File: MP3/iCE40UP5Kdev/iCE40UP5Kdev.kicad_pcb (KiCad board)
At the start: 2 copper layers, 27.9 x 52.4 mm, 51 parts, among them J1 USB4105-GF-A, J2 Left, J3 Right, U1 W25Q32JV, U2 MIC5365-1-2YD5, U3 MIC5318-3-3YD5, U4 ICE40UP5K-SG48ITR, X1 IQXO-791

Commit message: Rev.1 Layout
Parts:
- moved S3 42.7 mm to (164.3, 85.6)
- moved C1 41.3 mm to (153.8, 95.9)
- moved R2 39.8 mm to (163.6, 101.3), turned to 90 degrees
- moved R5 38.8 mm to (157.7, 70.5), turned to 90 degrees
- moved R7 33.4 mm to (166.4, 68.5), turned to -90 degrees
- moved C2 33.2 mm to (151.2, 92.0), turned to -90 degrees
- moved C13 32.8 mm to (158.2, 73.0), turned to -90 degrees
- moved C7 32.0 mm to (154.0, 70.6), turned to 90 degrees
- moved D1 31.9 mm to (164.9, 65.7), turned to -90 degrees
- moved R12 28.7 mm to (154.2, 72.8), turned to -90 degrees
- moved R9 27.9 mm to (165.4, 68.5), turned to -90 degrees
- moved R8 27.1 mm to (164.4, 68.5), turned to -90 degrees
- moved C10 26.7 mm to (159.2, 83.9), turned to 90 degrees
- moved R20 25.8 mm to (164.3, 82.6)
- moved R6 24.9 mm to (156.6, 70.5), turned to 90 degrees
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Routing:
- net +5V: track 53.1 -> 195.8 mm, vias 0 -> 2
- net +3V3: track 115.5 -> 204.9 mm, vias 0 -> 11
- net Net-(J1-D--PadA7): track 2.70 -> 81.5 mm, vias 0 -> 2
- net Net-(J1-D+-PadA6): track 5.57 -> 70.7 mm, vias 2 -> 7
- net /RGB2: track 0.00 -> 59.1 mm, vias 0 -> 5
- net /RGB1: track 0.00 -> 56.6 mm, vias 0 -> 5
- net /RGB0: track 0.00 -> 51.9 mm, vias 0 -> 5
- net GND: track 18.9 -> 56.0 mm, vias 7 -> 24
- net /IOT_48b: track 0.00 -> 32.7 mm, vias 0 -> 2
- net /IOT_45a_G1: track 0.00 -> 30.4 mm
- net /IOT_46b_G0: track 0.00 -> 30.3 mm
- net /IOT_44b: track 0.00 -> 26.6 mm
- net Net-(U1-~{CS}): track 0.00 -> 25.1 mm, vias 0 -> 2
- net +1V2: track 3.07 -> 27.7 mm, vias 0 -> 4
- net Net-(U1-DO/IO1): track 0.00 -> 23.9 mm, vias 0 -> 2
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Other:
- board size 27.9 x 52.4 mm -> 29.6 x 52.2 mm

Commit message: Final Design with PinHeader Labels + Graphics
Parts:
- added G***: LOGO, LOGO, B.Cu at (154.9, 95.2)
- added OlinLogo: G***, Eclectronics:OlinLogo, F.Cu at (165.7, 101.7)
- moved C14 8.14 mm to (157.4, 83.8), turned to 90 degrees
- moved U2 5.13 mm to (153.5, 97.7)
- moved C1 5.01 mm to (153.4, 100.9)
- moved R20 4.80 mm to (164.3, 87.4), turned to 180 degrees
- moved C2 3.55 mm to (153.4, 94.8), turned to 0 degrees
- moved R18 1.97 mm to (157.0, 86.3)
- moved R2 1.69 mm to (162.6, 99.9)
- moved C15 1.67 mm to (154.6, 87.1)
- moved R19 1.53 mm to (161.7, 69.5)
- moved S3 1.28 mm to (164.3, 84.3)
- moved D4 1.12 mm to (153.0, 83.0)
- moved C11 1.11 mm to (153.9, 82.9)
- moved C9 0.66 mm to (162.2, 73.9), turned to -90 degrees
- moved C10 0.46 mm to (159.2, 83.4)
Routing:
- net +5V: track 195.8 -> 181.3 mm
- net +3V3: track 204.9 -> 195.7 mm, vias 11 -> 12
- net /IOT_45a_G1: track 30.4 -> 34.0 mm
- net /IOT_50b: track 10.0 -> 13.3 mm, vias 0 -> 2
- net /IOT_37a: track 18.8 -> 16.5 mm
- net /IOT_49a: track 30.6 -> 32.6 mm
- net /IOT_51a: track 17.0 -> 19.0 mm
- net /IOB_3b_G6: track 29.2 -> 31.2 mm
- net /IOB_2a: track 19.8 -> 21.7 mm
- net /IOB_5a: track 26.5 -> 28.4 mm
- net GND: track 56.0 -> 54.2 mm, vias 24 -> 25
- net /IOB_0a: track 24.3 -> 26.1 mm
- net +1V2: track 27.7 -> 29.5 mm
- net Net-(D4-K): track 4.32 -> 2.80 mm
- net /IOB_4a: track 17.6 -> 19.1 mm
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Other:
- board size 29.6 x 52.2 mm -> 32.2 x 52.2 mm
- board text added: "0A"
- board text added: "13B"
- board text added: "18A"
- board text added: "20A"
- board text added: "29b"
- board text added: "2A"
- board text added: "31b"
- board text added: "36b"
- board text added: "37a"
- board text added: "38b"
- board text added: "39a"
- board text added: "3B G6"
- board text added: "3V3"
- board text added: "41a"
- board text added: "42b"
- board text added: "43a"
- board text added: "44b"
- board text added: "45A G1"
- board text added: "46b G0"
- board text added: "48B"
- board text added: "49A"
- board text added: "4A"
- board text added: "5A"
- board text added: "5V"
- board text added: "6A"
- board text added: "8A"
- board text added: "9B"
- board text added: "BOOT"
- board text added: "By"
- board text added: "Designed Jun Park"
- board text added: "GND"
- board text added: "LED"
- board text added: "PWR"
- board text added: "RGB"
- board text added: "RGB 0"
- board text added: "RGB 1"
- board text added: "RGB 2"
- board text added: "RST"
- board text added: "Rev 1.0"
- board text added: "SW"
- board text added: "ice40 FPGA Dev Board"

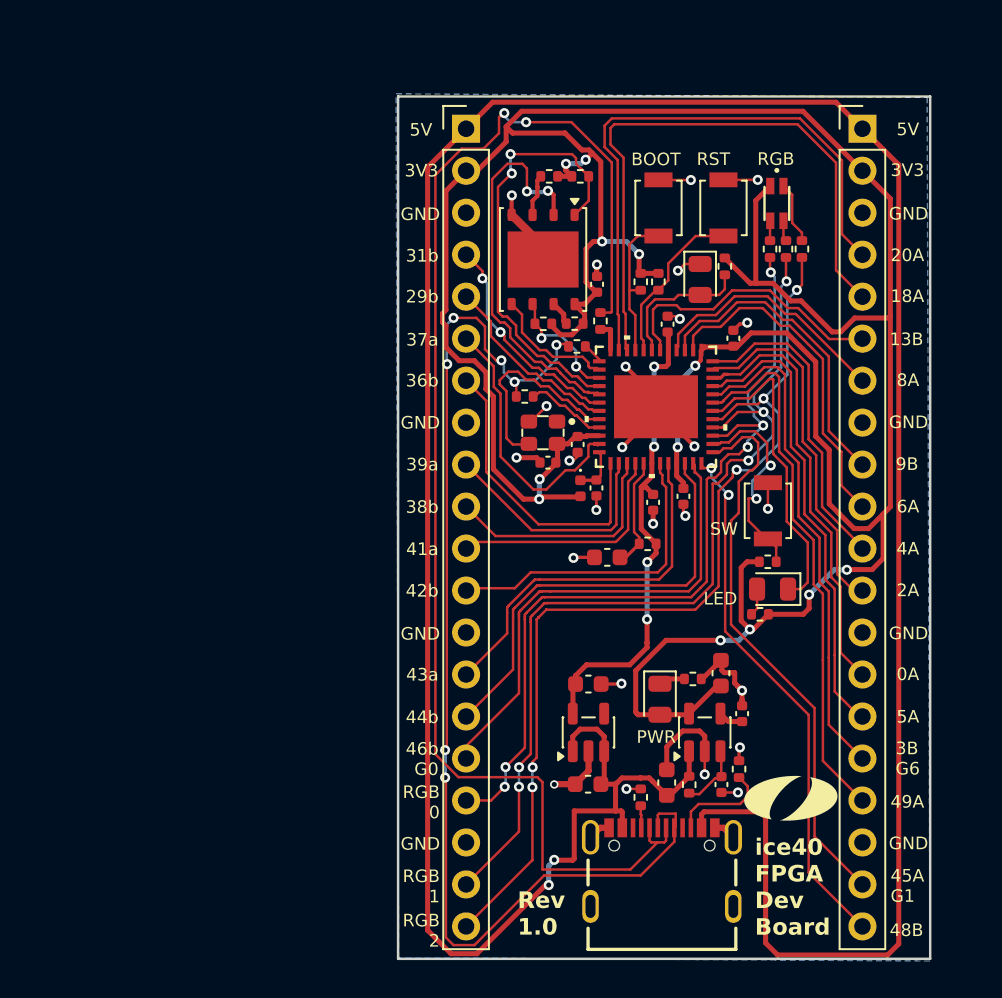
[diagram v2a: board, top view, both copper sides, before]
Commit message: Implementing Feedback
- Made USB D+, D- on one plane and made the path shorter
- Used correct footprint for FPGA Chip
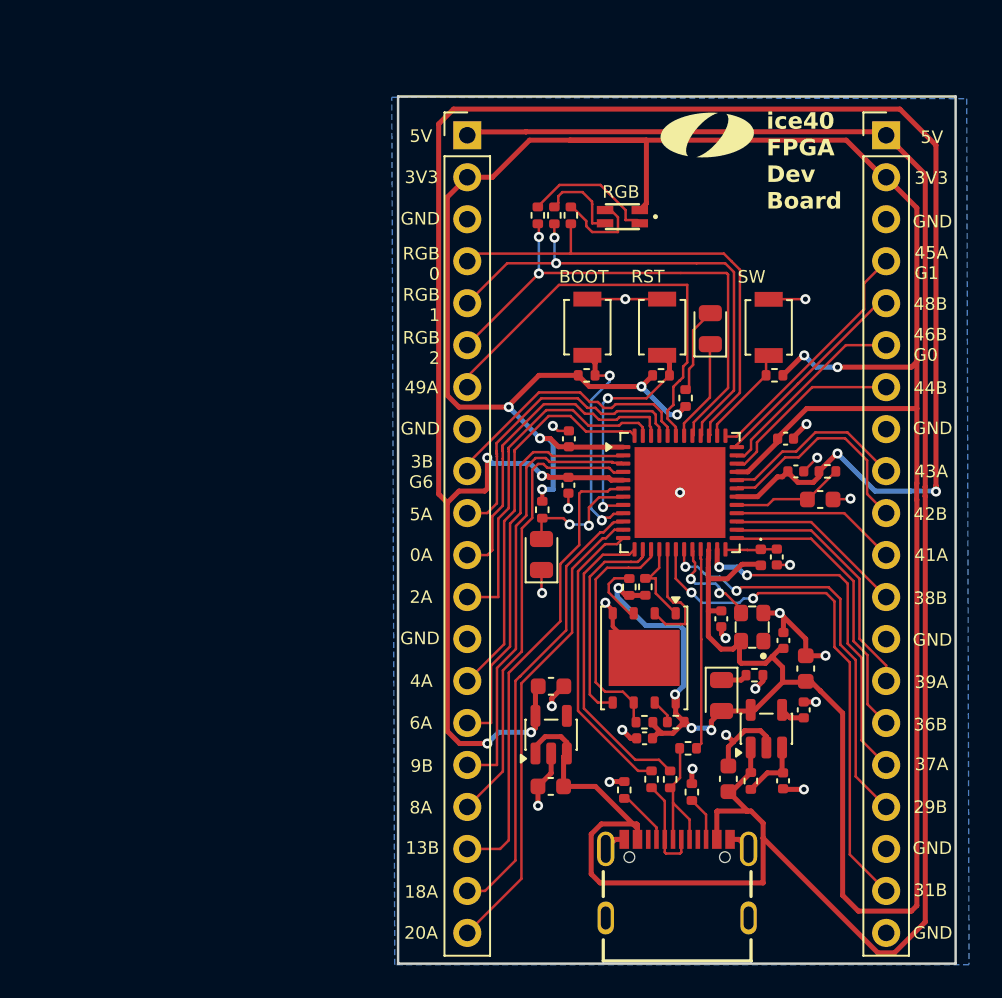
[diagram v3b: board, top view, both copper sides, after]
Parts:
- U4: footprint Eclectronics:QFN48_L-ASC10_ICE40ULTRAPLUS_MACHXO2_LAT -> Package_DFN_QFN:QFN-48-1EP_7x7mm_P0.5mm_EP5.6x5.6mm
- moved OlinLogo 40.4 mm to (160.6, 61.6)
- moved R12 27.9 mm to (157.3, 100.6), turned to 90 degrees
- moved C7 27.6 mm to (156.8, 98.1), turned to 180 degrees
- moved R10 26.8 mm to (158.4, 100.6), turned to 90 degrees
- moved R15 25.3 mm to (155.9, 88.9), turned to -90 degrees
- moved R13 25.1 mm to (156.9, 88.9), turned to 90 degrees
- moved R14 24.9 mm to (156.8, 97.1)
- moved R16 24.9 mm to (158.7, 97.1)
- moved U1 24.9 mm to (156.8, 93.2)
- moved R11 23.5 mm to (159.5, 98.7)
- moved D5 19.2 mm to (150.6, 87.0), turned to 90 degrees
- moved R19 18.4 mm to (150.7, 84.2)
- moved C8 17.9 mm to (165.2, 92.2), turned to 90 degrees
- moved X1 17.3 mm to (163.4, 91.3), turned to 90 degrees
- moved D3 16.2 mm to (160.8, 73.3), turned to 90 degrees
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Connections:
- J2 pad 10: /IOT_38b -> /IOB_5a
- J2 pad 11: /IOT_41a -> /IOB_0a
- J2 pad 12: /IOT_42b -> /IOB_2a
- J2 pad 14: /IOT_43a -> /IOB_4a
- J2 pad 15: /IOT_44b -> /IOB_6a
- J2 pad 16: /IOT_46b_G0 -> /IOB_9b
- J2 pad 17: /RGB0 -> /IOB_8a
- J2 pad 18: GND -> /IOB_13b
- J2 pad 19: /RGB1 -> /IOB_18a
- J2 pad 20: /RGB2 -> /IOB_20a
- J2 pad 4: /IOB_31b -> /RGB0
- J2 pad 5: /IOB_29b -> /RGB1
- J2 pad 6: /IOT_37a -> /RGB2
- J2 pad 7: /IOT_36b -> /IOT_49a
- J2 pad 9: /IOT_39a -> /IOB_3b_G6
- J3 pad 10: /IOB_6a -> /IOT_42b
- J3 pad 11: /IOB_4a -> /IOT_41a
- J3 pad 12: /IOB_2a -> /IOT_38b
- J3 pad 14: /IOB_0a -> /IOT_39a
- J3 pad 15: /IOB_5a -> /IOT_36b
- J3 pad 16: /IOB_3b_G6 -> /IOT_37a
- J3 pad 17: /IOT_49a -> /IOB_29b
- J3 pad 19: /IOT_45a_G1 -> /IOB_31b
- J3 pad 20: /IOT_48b -> GND
- J3 pad 4: /IOB_20a -> /IOT_45a_G1
- J3 pad 5: /IOB_18a -> /IOT_48b
- J3 pad 6: /IOB_13b -> /IOT_46b_G0
- J3 pad 7: /IOB_8a -> /IOT_44b
- J3 pad 9: /IOB_9b -> /IOT_43a
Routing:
- net +1V2: track 29.5 -> 126.2 mm, vias 4 -> 6
- net Net-(J1-D--PadA7): track 81.7 -> 6.20 mm, vias 2 -> 0
- net Net-(J1-D+-PadA6): track 70.7 -> 8.66 mm, vias 7 -> 0
- net +5V: track 181.3 -> 130.2 mm, vias 2 -> 0
- net /RGB2: track 59.5 -> 31.4 mm, vias 5 -> 2
- net /RGB1: track 56.6 -> 30.6 mm, vias 5 -> 2
- net Net-(U1-~{CS}): track 26.4 -> 5.42 mm, vias 2 -> 0
- net /RGB0: track 51.3 -> 30.6 mm, vias 5 -> 0
- net /IOT_48b: track 32.5 -> 12.8 mm, vias 2 -> 0
- net /IOT_45a_G1: track 34.0 -> 15.0 mm
- net /IOB_31b: track 13.7 -> 31.2 mm
- net Net-(U4-IOB_24a): track 1.28 -> 18.6 mm
- net /IOT_46b_G0: track 29.5 -> 12.2 mm
- net Net-(U1-DO/IO1): track 24.0 -> 7.32 mm, vias 2 -> 0
- net Net-(U4-IOB_22a): track 1.85 -> 18.0 mm
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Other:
- board size 32.2 x 52.2 mm -> 33.7 x 52.5 mm
- board text added: "29B"
- board text added: "31B"
- board text added: "36B"
- board text added: "37A"
- board text added: "38B"
- board text added: "39A"
- board text added: "41A"
- board text added: "42B"
- board text added: "43A"
- board text added: "44B"
- board text added: "46B G0"
- board text removed: "29b"
- board text removed: "31b"
- board text removed: "36b"
- board text removed: "37a"
- board text removed: "38b"
- board text removed: "39a"
- board text removed: "41a"
- board text removed: "42b"
- board text removed: "43a"
- board text removed: "44b"
- board text removed: "46b G0"
- board text removed: "LED"
- board text removed: "PWR"
- board text removed: "Rev 1.0"
